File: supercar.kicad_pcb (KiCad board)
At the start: 2 copper layers, 55 parts, among them U1 74HC283, U2 74HC574, U3 74HC154, U4 74HC574, U5 74HC21, U6 74HC02, U7 74HC04, U8 NE555D

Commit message: add pcb
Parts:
- BT1: moved to B.Cu
- JP1: value Power on -> PWR
- moved U3 63.7 mm to (125.7, 58.6), turned to -90 degrees
- moved D12 61.0 mm to (123.2, 48.5), turned to -90 degrees
- moved D16 60.7 mm to (138.4, 48.5), turned to -90 degrees
- moved D11 56.2 mm to (119.4, 48.5), turned to -90 degrees
- moved D15 55.7 mm to (134.6, 48.5), turned to -90 degrees
- moved C1 55.6 mm to (136.5, 58.7), turned to -90 degrees
- moved D6 54.6 mm to (100.3, 48.5), turned to -90 degrees
- moved C6 53.6 mm to (134.0, 70.1), turned to -90 degrees
- moved R14 53.4 mm to (130.8, 43.5), turned to 90 degrees
- moved C7 53.2 mm to (134.0, 77.8), turned to -90 degrees
- moved D10 51.4 mm to (115.6, 48.5), turned to -90 degrees
- moved D14 50.7 mm to (130.8, 48.5), turned to -90 degrees
- moved D5 50.5 mm to (96.5, 48.5), turned to -90 degrees
- moved R13 48.4 mm to (127.0, 43.5), turned to 90 degrees
- moved D9 46.7 mm to (111.8, 48.5), turned to -90 degrees
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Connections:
- U3 pad 1: Net-(D1-A) -> Net-(D16-A)
- U3 pad 10: Net-(D10-A) -> Net-(D7-A)
- U3 pad 11: Net-(D11-A) -> Net-(D6-A)
- U3 pad 13: Net-(D12-A) -> Net-(D5-A)
- U3 pad 14: Net-(D13-A) -> Net-(D4-A)
- U3 pad 15: Net-(D14-A) -> Net-(D3-A)
- U3 pad 16: Net-(D15-A) -> Net-(D2-A)
- U3 pad 17: Net-(D16-A) -> Net-(D1-A)
- U3 pad 2: Net-(D2-A) -> Net-(D15-A)
- U3 pad 3: Net-(D3-A) -> Net-(D14-A)
- U3 pad 4: Net-(D4-A) -> Net-(D13-A)
- U3 pad 5: Net-(D5-A) -> Net-(D12-A)
- U3 pad 6: Net-(D6-A) -> Net-(D11-A)
- U3 pad 7: Net-(D7-A) -> Net-(D10-A)
- U3 pad 8: Net-(D8-A) -> Net-(D9-A)
- U3 pad 9: Net-(D9-A) -> Net-(D8-A)
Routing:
- net GND: track 0.00 -> 289.8 mm, vias 0 -> 5
- net +3V3: track 0.00 -> 167.3 mm, vias 0 -> 1
- net Net-(U1-A1): track 0.00 -> 73.4 mm, vias 0 -> 3
- net Net-(U1-A2): track 0.00 -> 64.1 mm, vias 0 -> 3
- net Net-(U1-A4): track 0.00 -> 63.4 mm, vias 0 -> 2
- net Net-(U1-A3): track 0.00 -> 60.4 mm
- net Net-(U4-D1): track 0.00 -> 57.9 mm, vias 0 -> 3
- net Net-(U4-Cp): track 0.00 -> 49.8 mm, vias 0 -> 2
- net Net-(D1-A): track 0.00 -> 49.6 mm, vias 0 -> 2
- net Net-(D2-A): track 0.00 -> 43.2 mm, vias 0 -> 2
- net Net-(D3-A): track 0.00 -> 39.2 mm, vias 0 -> 2
- net Net-(U8-CV): track 0.00 -> 36.0 mm, vias 0 -> 2
- net Net-(D4-A): track 0.00 -> 33.2 mm, vias 0 -> 2
- net Net-(U5-Pad8): track 0.00 -> 32.3 mm, vias 0 -> 2
- net Net-(U5-Pad9): track 0.00 -> 30.1 mm, vias 0 -> 2
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- added copper zone on B.Cu, net GND
- added copper zone on F.Cu, net GND
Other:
- board outline added: 63.5 x 48.9 mm

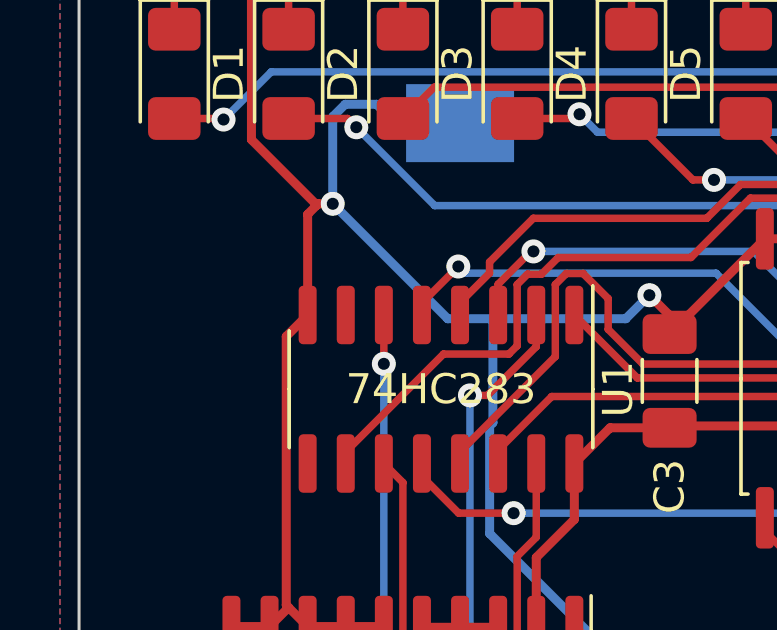
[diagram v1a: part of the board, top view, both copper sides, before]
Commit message: Carry bit must be set to 0
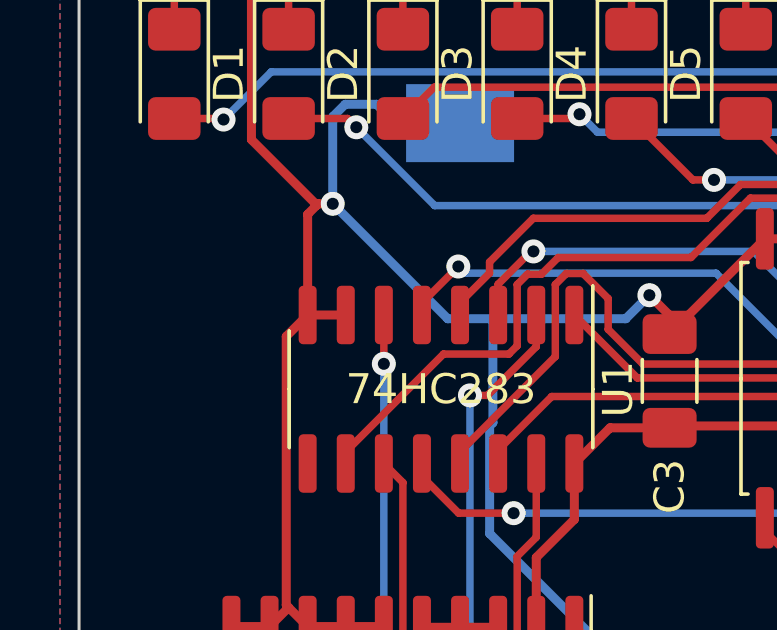
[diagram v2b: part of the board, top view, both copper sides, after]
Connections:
- U1 pad 7: unconnected-(U1-C0-Pad7) -> GND
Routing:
- net GND: track 289.8 -> 291.1 mm

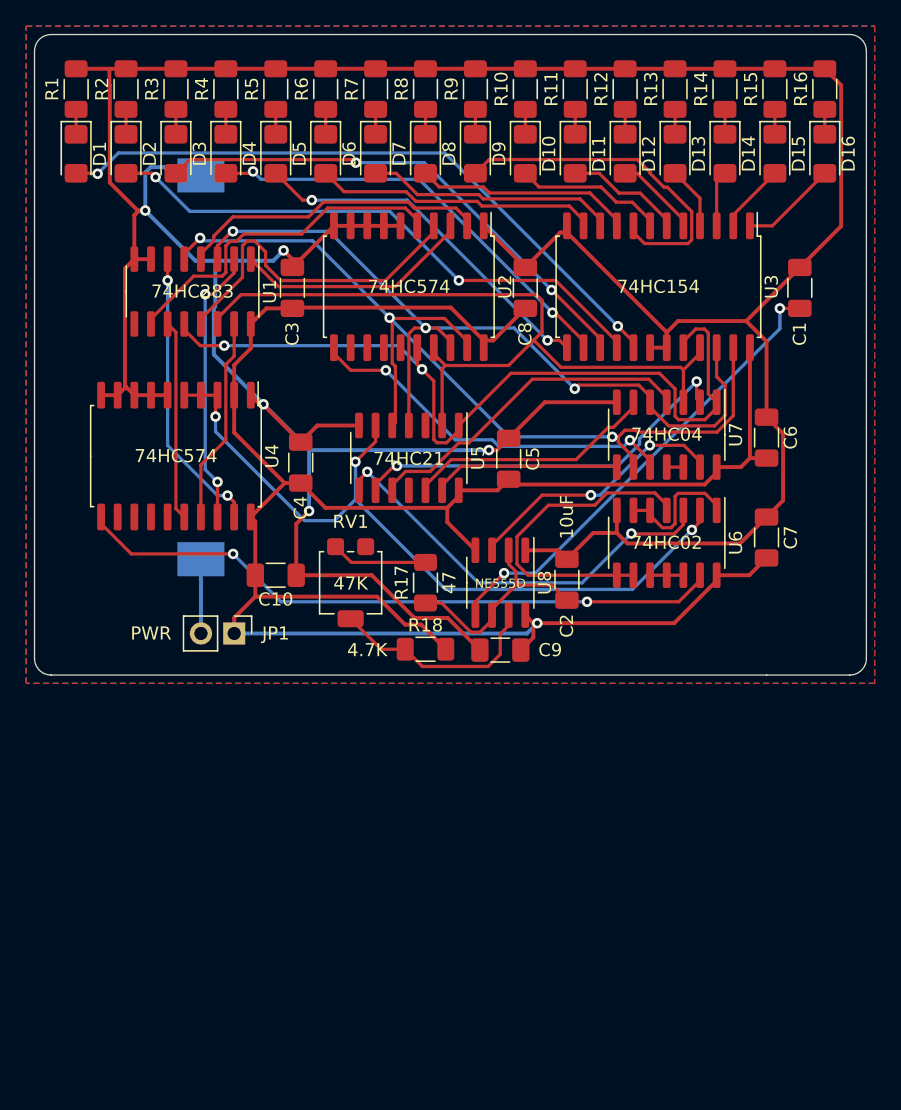
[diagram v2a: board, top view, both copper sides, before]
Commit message: Fix led orientation and connection
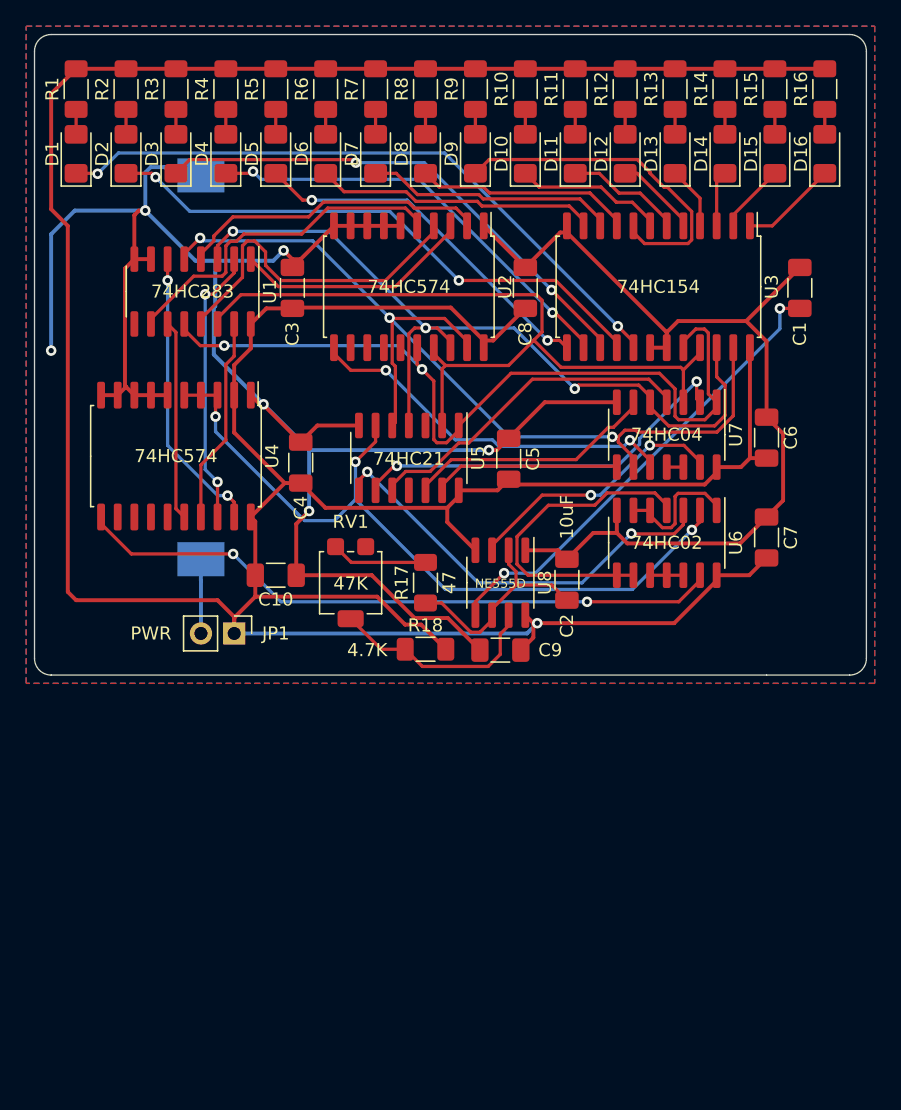
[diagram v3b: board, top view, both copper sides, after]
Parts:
- turned D1 to 90 degrees
- turned D10 to 90 degrees
- turned D11 to 90 degrees
- turned D12 to 90 degrees
- turned D13 to 90 degrees
- turned D14 to 90 degrees
- turned D15 to 90 degrees
- turned D16 to 90 degrees
- turned D2 to 90 degrees
- turned D3 to 90 degrees
- turned D4 to 90 degrees
- turned D5 to 90 degrees
- turned D6 to 90 degrees
- turned D7 to 90 degrees
- turned D8 to 90 degrees
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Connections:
- R1 pad 1: Net-(D1-K) -> Net-(D1-A)
- R1 pad 2: GND -> +3V3
- R10 pad 1: Net-(D10-K) -> Net-(D10-A)
- R10 pad 2: GND -> +3V3
- R11 pad 1: Net-(D11-K) -> Net-(D11-A)
- R11 pad 2: GND -> +3V3
- R12 pad 1: Net-(D12-K) -> Net-(D12-A)
- R12 pad 2: GND -> +3V3
- R13 pad 1: Net-(D13-K) -> Net-(D13-A)
- R13 pad 2: GND -> +3V3
- R14 pad 1: Net-(D14-K) -> Net-(D14-A)
- R14 pad 2: GND -> +3V3
- R15 pad 1: Net-(D15-K) -> Net-(D15-A)
- R15 pad 2: GND -> +3V3
- R16 pad 1: Net-(D16-K) -> Net-(D16-A)
- R16 pad 2: GND -> +3V3
- R2 pad 1: Net-(D2-K) -> Net-(D2-A)
- R2 pad 2: GND -> +3V3
- R3 pad 1: Net-(D3-K) -> Net-(D3-A)
- R3 pad 2: GND -> +3V3
- R4 pad 1: Net-(D4-K) -> Net-(D4-A)
- R4 pad 2: GND -> +3V3
- R5 pad 1: Net-(D5-K) -> Net-(D5-A)
- R5 pad 2: GND -> +3V3
- R6 pad 1: Net-(D6-K) -> Net-(D6-A)
- R6 pad 2: GND -> +3V3
- R7 pad 1: Net-(D7-K) -> Net-(D7-A)
- R7 pad 2: GND -> +3V3
- R8 pad 1: Net-(D8-K) -> Net-(D8-A)
- R8 pad 2: GND -> +3V3
- R9 pad 1: Net-(D9-K) -> Net-(D9-A)
- R9 pad 2: GND -> +3V3
- U3 pad 1: Net-(D16-A) -> Net-(D16-K)
- U3 pad 10: Net-(D7-A) -> Net-(D7-K)
- U3 pad 11: Net-(D6-A) -> Net-(D6-K)
- U3 pad 13: Net-(D5-A) -> Net-(D5-K)
- U3 pad 14: Net-(D4-A) -> Net-(D4-K)
- U3 pad 15: Net-(D3-A) -> Net-(D3-K)
- U3 pad 16: Net-(D2-A) -> Net-(D2-K)
- U3 pad 17: Net-(D1-A) -> Net-(D1-K)
- U3 pad 2: Net-(D15-A) -> Net-(D15-K)
- U3 pad 3: Net-(D14-A) -> Net-(D14-K)
- U3 pad 4: Net-(D13-A) -> Net-(D13-K)
- U3 pad 5: Net-(D12-A) -> Net-(D12-K)
- U3 pad 6: Net-(D11-A) -> Net-(D11-K)
- U3 pad 7: Net-(D10-A) -> Net-(D10-K)
- U3 pad 8: Net-(D9-A) -> Net-(D9-K)
- U3 pad 9: Net-(D8-A) -> Net-(D8-K)
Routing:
- net +3V3: track 167.3 -> 280.5 mm
- net GND: track 291.1 -> 222.0 mm, vias 5 -> 6
- net Net-(D1-K): track 1.91 -> 49.6 mm, vias 0 -> 2
- net Net-(D1-A): track 49.6 -> 1.91 mm, vias 2 -> 0
- net Net-(D2-K): track 1.91 -> 43.2 mm, vias 0 -> 2
- net Net-(D2-A): track 43.2 -> 1.91 mm, vias 2 -> 0
- net Net-(D3-K): track 1.91 -> 39.2 mm, vias 0 -> 2
- net Net-(D3-A): track 39.2 -> 1.91 mm, vias 2 -> 0
- net Net-(D4-K): track 1.91 -> 33.2 mm, vias 0 -> 2
- net Net-(D4-A): track 33.2 -> 1.91 mm, vias 2 -> 0
- net Net-(D5-K): track 1.91 -> 27.7 mm, vias 0 -> 2
- net Net-(D5-A): track 27.7 -> 1.91 mm, vias 2 -> 0
- net Net-(D9-K): track 1.91 -> 26.2 mm
- net Net-(D9-A): track 26.2 -> 1.91 mm
- net Net-(D6-K): track 1.91 -> 21.6 mm
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
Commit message: Update the PCB to include a reset circuit
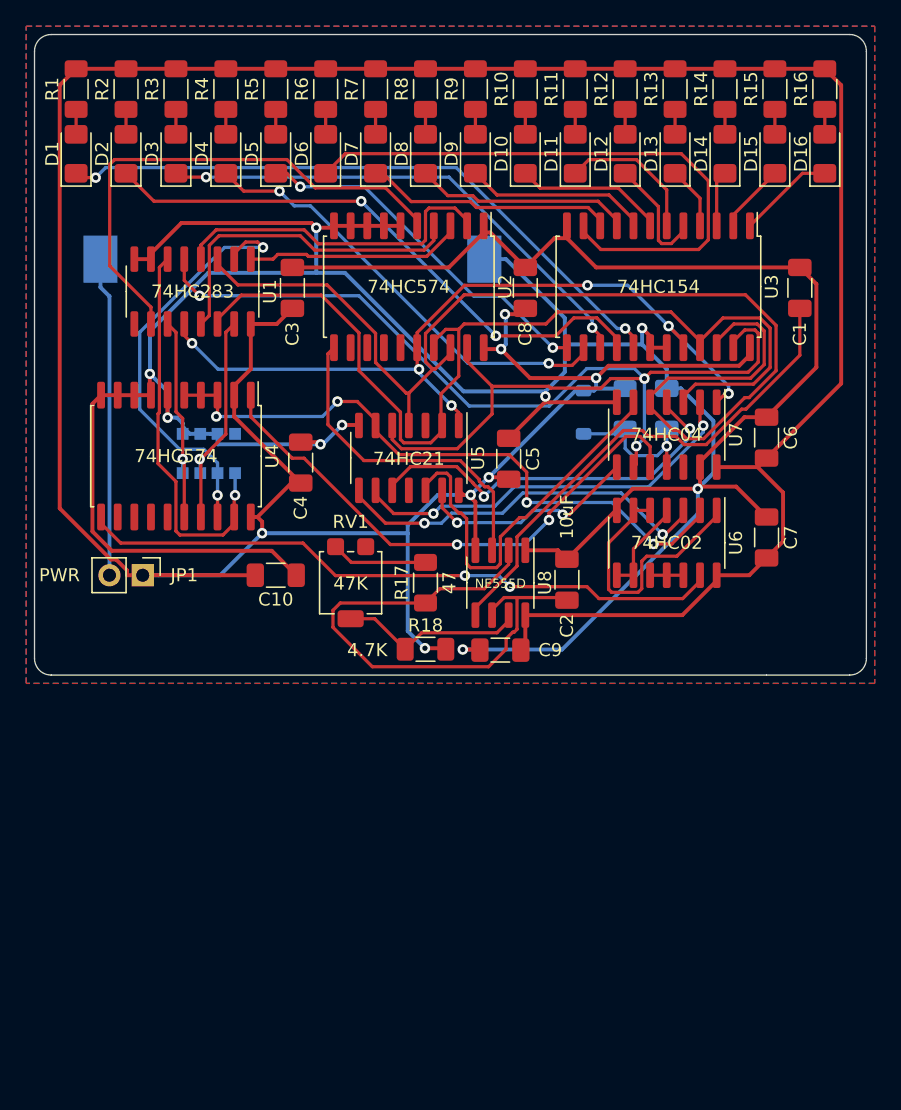
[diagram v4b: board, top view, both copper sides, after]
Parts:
- added C11: 1uF, Capacitor_SMD:C_1206_3216Metric_Pad1.33x1.80mm_HandSolder, B.Cu at (126.4, 67.9)
- added D17: 1N4148W, Diode_SMD:D_SOD-123, B.Cu at (120.0, 68.2)
- added R19: 100K, Resistor_SMD:R_1206_3216Metric_Pad1.30x1.75mm_HandSolder, B.Cu at (123.2, 67.9)
- added RN1: 10K, Resistor_SMD:R_Array_Convex_4x1206, B.Cu at (91.4, 71.3)
- moved BT1 10.8 mm to (97.8, 56.5), turned to 0 degrees
- moved JP1 8.28 mm to (86.4, 80.6)
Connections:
- U4 pad 1: GND -> /RST
- U7 pad 10: /CLK -> /RST
- U7 pad 11: Net-(U7-Pad11) -> Net-(D17-A)
- U7 pad 12: Net-(U7-Pad11) -> unconnected-(U7-Pad12)
- U7 pad 13: Net-(U8-Q) -> GND
- U8 pad 3: Net-(U8-Q) -> /CLK
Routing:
- net GND: track 222.0 -> 284.7 mm, vias 6 -> 9
- net /RST: track 0.00 -> 41.8 mm, vias 0 -> 2
- net Net-(U1-A2): track 64.1 -> 93.9 mm, vias 3 -> 0
- net Net-(U8-THR): track 17.1 -> 43.2 mm
- net Net-(D6-K): track 21.6 -> 46.1 mm
- net Net-(U8-Q): track 20.4 -> 0.00 mm, vias 2 -> 0
- net Net-(BT1-+): track 5.67 -> 24.4 mm
- net Net-(U1-A1): track 73.4 -> 91.5 mm
- net Net-(U6-Pad4): track 25.0 -> 7.27 mm
- net Net-(U1-A3): track 60.4 -> 75.2 mm
- net Net-(U1-S4): track 26.2 -> 39.5 mm
- net Net-(D9-K): track 26.2 -> 14.0 mm
- net Net-(RN1-R3.2): track 21.3 -> 32.9 mm
- net Net-(D17-A): track 0.00 -> 11.2 mm, vias 0 -> 1
- net Net-(U5-Pad12): track 19.1 -> 29.7 mm
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
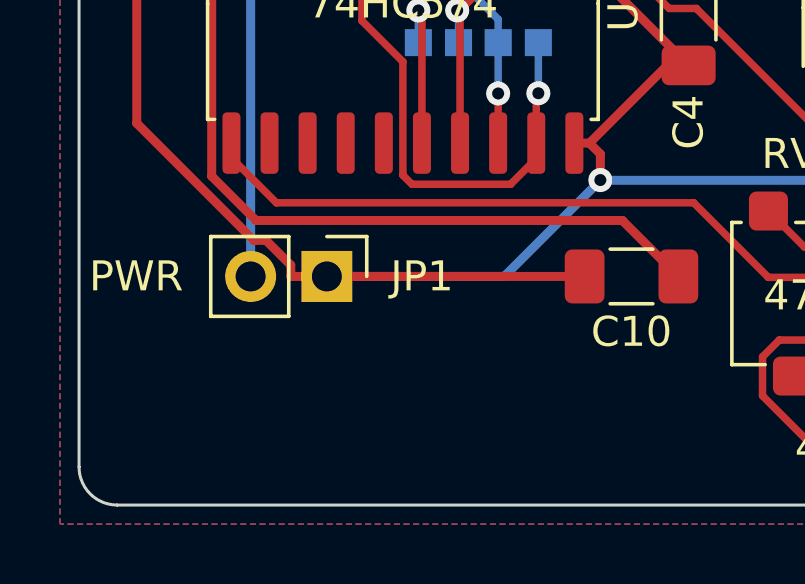
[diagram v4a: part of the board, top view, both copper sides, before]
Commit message: Reorganize silkscreen a bit
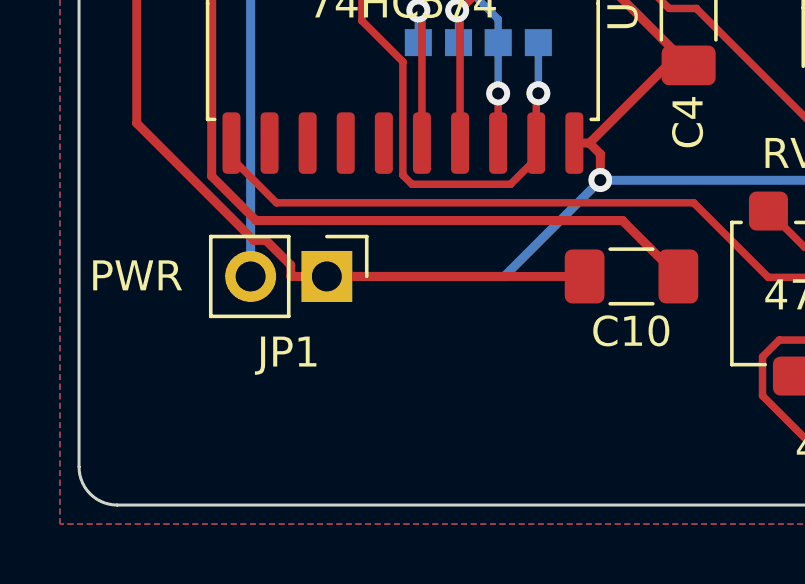
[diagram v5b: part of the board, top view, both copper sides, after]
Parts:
- BT1: value Battery_Cell -> CR2032
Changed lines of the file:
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@@
     (property "ki_keywords" "Jumper SPST")
     (attr through_hole)
-    (fp_text reference "JP1" (at 0 -3.17) (layer "F.SilkS")
+    (fp_text reference "JP1" (at 2.54 1.275) (layer "F.SilkS")
         (effects (font (size 1 1) (thickness 0.15)))
     )
@@
         (effects (font (size 1 1) (thickness 0.15)) (justify mirror))
     )
-    (fp_text value "Battery_Cell" (at 0 11.75) (layer "B.Fab")
-        (effects (font (size 1 1) (thickness 0.15)) (justify mirror))
-    )
-    (fp_text user "${REFERENCE}" (at 0 0) (layer "B.Fab")
+    (fp_text value "CR2032" (at -14.605 6.985) (layer "B.SilkS")
+        (effects (font (size 1 1) (thickness 0.15)) (justify mirror))
+    )
+    (fp_text user "${REFERENCE}" (at -13.335 -5.08) (layer "B.SilkS")
         (effects (font (size 1 1) (thickness 0.15)) (justify mirror))
     )
@@
         (effects (font (size 1 1) (thickness 0.15)) (justify mirror))
     )
-    (fp_text value "10K" (at 0 -3.5 90) (layer "B.Fab")
+    (fp_text value "10K" (at 0 -3.5 90) (layer "B.SilkS")
         (effects (font (size 1 1) (thickness 0.15)) (justify mirror))
     )
@@
         (effects (font (size 1 1) (thickness 0.15)) (justify mirror))
     )
-    (fp_text value "1uF" (at 4.445 0 90) (layer "B.Fab")
+    (fp_text value "1uF" (at 4.445 0 90) (layer "B.SilkS")
         (effects (font (size 1 1) (thickness 0.15)) (justify mirror))
     )
@@
         (effects (font (size 1 1) (thickness 0.15)) (justify mirror))
     )
-    (fp_text value "100K" (at 4.445 0 90) (layer "B.Fab")
-        (effects (font (size 1 1) (thickness 0.15)) (justify mirror))
-    )
+    (fp_text value "100K" (at 4.445 0 90) (layer "B.SilkS")
+        (effects (font (size 1 1) (thickness 0.15)) (justify mirror))
+    )

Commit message: Update schematic and PCB
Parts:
- removed JP1: PWR, Connector_PinHeader_2.54mm:PinHeader_1x02_P2.54mm_Vertical
- added SW1: Power, Button_Switch_THT:SW_Slide_1P2T_CK_OS102011MS2Q, F.Cu at (85.7, 83.2)
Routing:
- net Net-(BT1-+): track 24.4 -> 27.7 mm
- net +3V3: track 290.2 -> 293.4 mm

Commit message: Slight change to PCB
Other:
- board text added: "Rev. 0"
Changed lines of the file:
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@@
   (gr_line (start 79.375 88.265) (end 133.985 88.265)
     (stroke (width 0.1) (type default)) (layer "Edge.Cuts"))
+  (gr_text "Rev. 0" (at 136.525 87.63) (layer "F.SilkS")
+    (effects (font (size 0.8 0.8) (thickness 0.1) bold) (justify left bottom))
+  )
   (segment (start 84.455 79.375) (end 84.455 59.9819) (width 0.3) (layer "B.Cu") (net 1))
   (segment (start 84.455 59.9819) (end 83.14 58.6669) (width 0.3) (layer "B.Cu") (net 1))
